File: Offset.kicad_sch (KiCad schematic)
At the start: 18 parts, among them J1 Conn_01x02, J2 Conn_01x02, J3 Conn_01x02, U1 LM358

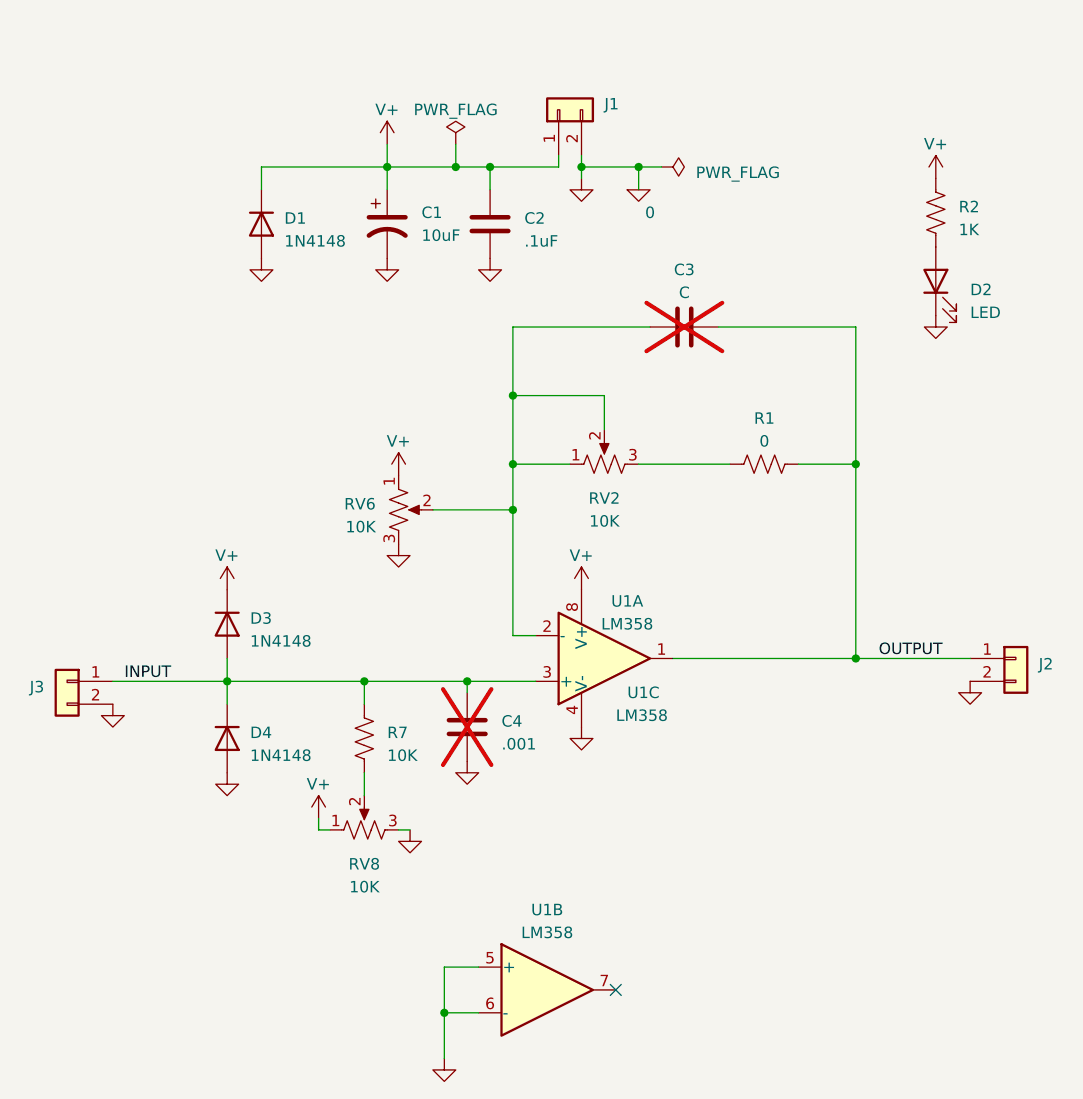
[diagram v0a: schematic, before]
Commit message: Remove zero reference
Seems to not be needed
Causes an ERC warning
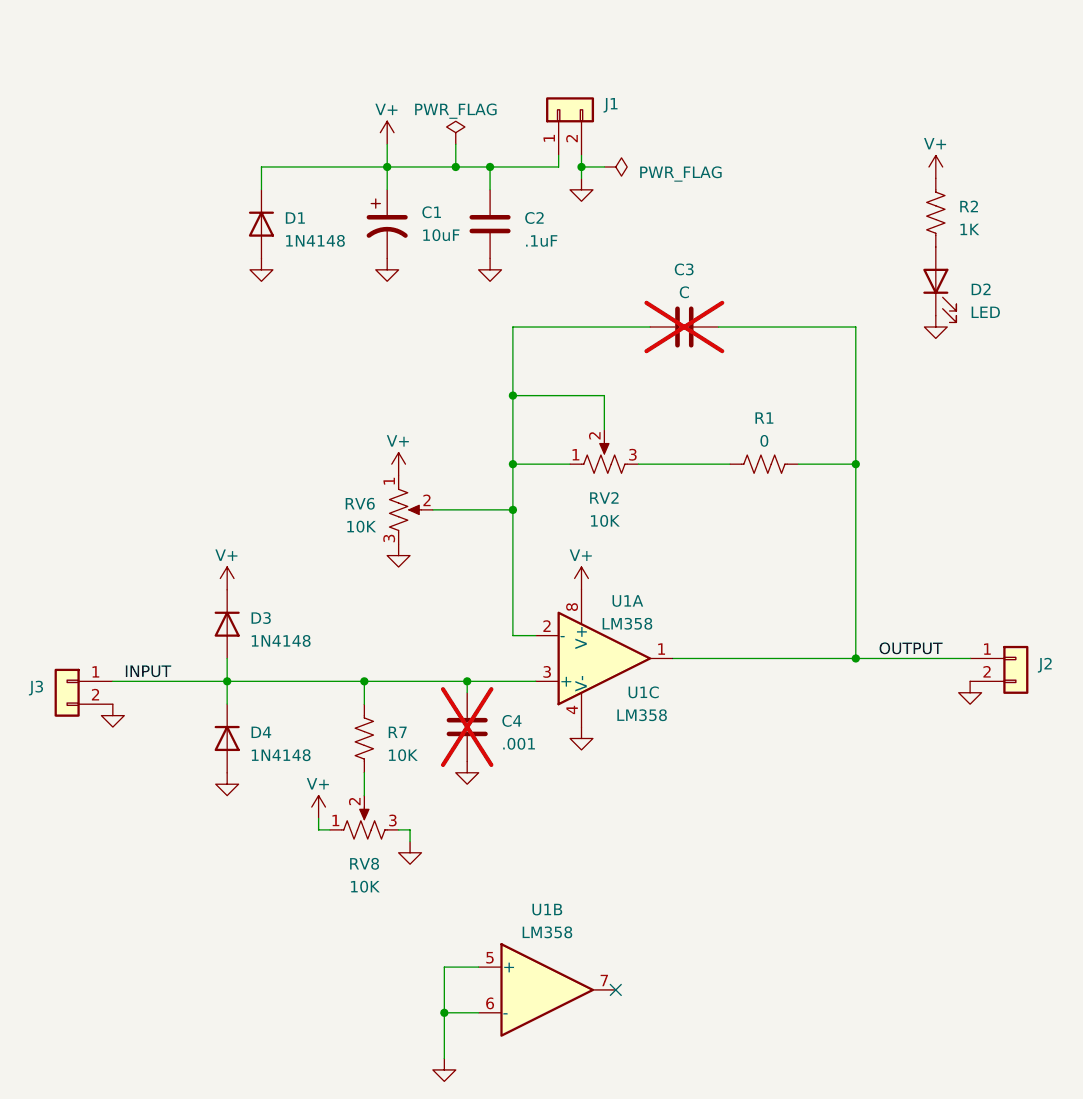
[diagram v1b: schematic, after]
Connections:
- net 0 renamed GND
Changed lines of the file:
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@@
   (junction (at 137.16 107.95) (diameter 0) (color 0 0 0 0)
-  )
-  (junction (at 156.21 50.8) (diameter 0) (color 0 0 0 0)
   )
   (junction (at 139.7 50.8) (diameter 0) (color 0 0 0 0)
@@
     (stroke (width 0) (type default))
   )
-  (wire (pts (xy 149.86 50.8) (xy 156.21 50.8))
+  (wire (pts (xy 149.86 50.8) (xy 152.4 50.8))
     (stroke (width 0) (type default))
   )
@@
     (stroke (width 0) (type default))
   )
+  (wire (pts (xy 130.81 124.46) (xy 130.81 125.73))
+    (stroke (width 0) (type default))
+  )
+  (wire (pts (xy 129.54 124.46) (xy 130.81 124.46))
+    (stroke (width 0) (type default))
+  )
   (wire (pts (xy 142.24 88.9) (xy 142.24 83.82))
     (stroke (width 0) (type default))
@@
     (stroke (width 0) (type default))
   )
-  (wire (pts (xy 156.21 50.8) (xy 158.75 50.8))
-    (stroke (width 0) (type default))
-  )
   (wire (pts (xy 180.34 83.82) (xy 180.34 105.41))
     (stroke (width 0) (type default))
@@
     (stroke (width 0) (type default))
   )
-  (wire (pts (xy 156.21 50.8) (xy 156.21 53.34))
-    (stroke (width 0) (type default))
-  )
   (wire (pts (xy 110.49 105.41) (xy 110.49 107.95))
     (stroke (width 0) (type default))
@@
   )
   (wire (pts (xy 142.24 68.58) (xy 142.24 76.2))
-    (stroke (width 0) (type default))
-  )
-  (wire (pts (xy 129.54 124.46) (xy 130.81 124.46))
     (stroke (width 0) (type default))
   )
@@
     )
   )
-  (symbol (lib_id "power:PWR_FLAG") (at 158.75 50.8 270) (unit 1)
-    (in_bom yes) (on_board yes) (dnp no) (fields_autoplaced)
-    (property "Reference" "#FLG01" (at 160.655 50.8 0)
-      (effects (font (size 1.27 1.27)) hide)
-    )
-    (property "Value" "PWR_FLAG" (at 162.56 51.435 90)
-      (effects (font (size 1.27 1.27)) (justify left))
-    )
-    (property "Footprint" "" (at 158.75 50.8 0)
-      (effects (font (size 1.27 1.27)) hide)
-    )
-    (property "Datasheet" "~" (at 158.75 50.8 0)
+  (symbol (lib_id "power:PWR_FLAG") (at 152.4 50.8 270) (unit 1)
+    (in_bom yes) (on_board yes) (dnp no) (fields_autoplaced)
+    (property "Reference" "#FLG01" (at 154.305 50.8 0)
+      (effects (font (size 1.27 1.27)) hide)
+    )
+    (property "Value" "PWR_FLAG" (at 156.21 51.435 90)
+      (effects (font (size 1.27 1.27)) (justify left))
+    )
+    (property "Footprint" "" (at 152.4 50.8 0)
+      (effects (font (size 1.27 1.27)) hide)
+    )
+    (property "Datasheet" "~" (at 152.4 50.8 0)
       (effects (font (size 1.27 1.27)) hide)
     )
@@
     )
   )
-  (symbol (lib_id "power:GND") (at 130.81 124.46 0) (unit 1)
-    (in_bom yes) (on_board yes) (dnp no) (fields_autoplaced)
-    (property "Reference" "#PWR010" (at 130.81 130.81 0)
-      (effects (font (size 1.27 1.27)) hide)
-    )
-    (property "Value" "GND" (at 130.81 129.54 0)
-      (effects (font (size 1.27 1.27)) hide)
-    )
-    (property "Footprint" "" (at 130.81 124.46 0)
-      (effects (font (size 1.27 1.27)) hide)
-    )
-    (property "Datasheet" "" (at 130.81 124.46 0)
+  (symbol (lib_id "power:VCC") (at 149.86 97.79 0) (unit 1)
+    (in_bom yes) (on_board yes) (dnp no) (fields_autoplaced)
+    (property "Reference" "#PWR02" (at 149.86 101.6 0)
+      (effects (font (size 1.27 1.27)) hide)
+    )
+    (property "Value" "V+" (at 149.86 93.98 0)
+      (effects (font (size 1.27 1.27)))
+    )
+    (property "Footprint" "" (at 149.86 97.79 0)
+      (effects (font (size 1.27 1.27)) hide)
+    )
+    (property "Datasheet" "" (at 149.86 97.79 0)
+      (effects (font (size 1.27 1.27)) hide)
+    )
+    (pin "1")
+    (instances
+      (project "Offset"
+        (path "/b9c335b0-b204-4837-ad88-f803b4ac701f"
+          (reference "#PWR02") (unit 1)
+        )
+      )
+    )
+  )
+  (symbol (lib_id "power:GND") (at 130.81 125.73 0) (unit 1)
+    (in_bom yes) (on_board yes) (dnp no) (fields_autoplaced)
+    (property "Reference" "#PWR010" (at 130.81 132.08 0)
+      (effects (font (size 1.27 1.27)) hide)
+    )
+    (property "Value" "GND" (at 130.81 130.81 0)
+      (effects (font (size 1.27 1.27)) hide)
+    )
+    (property "Footprint" "" (at 130.81 125.73 0)
+      (effects (font (size 1.27 1.27)) hide)
+    )
+    (property "Datasheet" "" (at 130.81 125.73 0)
       (effects (font (size 1.27 1.27)) hide)
     )
@@
         )
       )
-    )
-  )
-  (symbol (lib_id "power:VCC") (at 149.86 97.79 0) (unit 1)
-    (in_bom yes) (on_board yes) (dnp no) (fields_autoplaced)
-    (property "Reference" "#PWR02" (at 149.86 101.6 0)
-      (effects (font (size 1.27 1.27)) hide)
-    )
-    (property "Value" "V+" (at 149.86 93.98 0)
-      (effects (font (size 1.27 1.27)))
-    )
-    (property "Footprint" "" (at 149.86 97.79 0)
-      (effects (font (size 1.27 1.27)) hide)
-    )
-    (property "Datasheet" "" (at 149.86 97.79 0)
-      (effects (font (size 1.27 1.27)) hide)
-    )
-    (pin "1")
-    (instances
-      (project "Offset"
-        (path "/b9c335b0-b204-4837-ad88-f803b4ac701f"
-          (reference "#PWR02") (unit 1)
-        )
-      )
-    )
-  )
-  (symbol (lib_id "Simulation_SPICE:0") (at 156.21 53.34 0) (unit 1)
-    (in_bom yes) (on_board yes) (dnp no)
-    (property "Reference" "#GND01" (at 156.21 55.88 0)
-      (effects (font (size 1.27 1.27)) hide)
-    )
-    (property "Value" "0" (at 157.48 55.88 0)
-      (effects (font (size 1.27 1.27)))
-    )
-    (property "Footprint" "" (at 156.21 53.34 0)
-      (effects (font (size 1.27 1.27)) hide)
-    )
-    (property "Datasheet" "~" (at 156.21 53.34 0)
-      (effects (font (size 1.27 1.27)) hide)
-    )
-    (pin "1")
-    (instances
-      (project "Offset"
-        (path "/b9c335b0-b204-4837-ad88-f803b4ac701f"
-          (reference "#GND01") (unit 1)
-        )
-      )

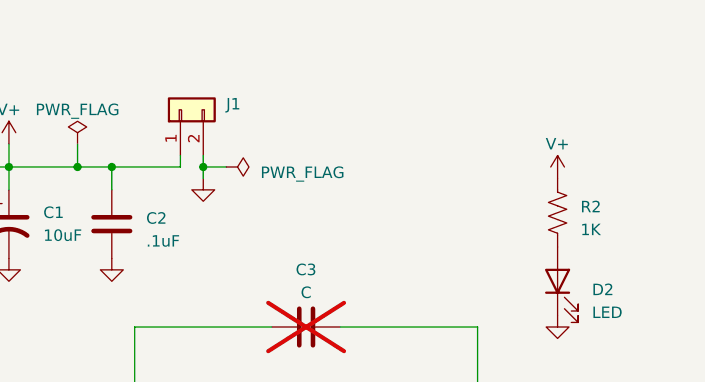
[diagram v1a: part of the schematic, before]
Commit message: Add power to simulation
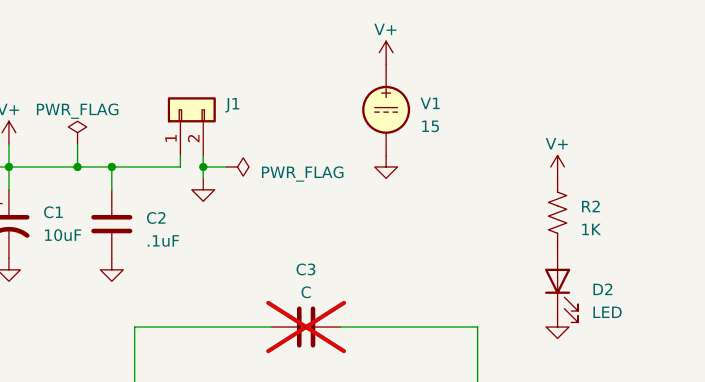
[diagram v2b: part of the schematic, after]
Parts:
- added V1: 15, symbol Simulation_SPICE:VDC
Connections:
- net GND: now also V1.2
- net VCC: now also V1.1
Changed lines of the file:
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@@
+    )
+  )
+  (symbol (lib_id "power:VCC") (at 170.18 39.37 0) (unit 1)
+    (in_bom yes) (on_board yes) (dnp no) (fields_autoplaced)
+    (property "Reference" "#PWR020" (at 170.18 43.18 0)
+      (effects (font (size 1.27 1.27)) hide)
+    )
+    (property "Value" "V+" (at 170.18 35.56 0)
+      (effects (font (size 1.27 1.27)))
+    )
+    (property "Footprint" "" (at 170.18 39.37 0)
+      (effects (font (size 1.27 1.27)) hide)
+    )
+    (property "Datasheet" "" (at 170.18 39.37 0)
+      (effects (font (size 1.27 1.27)) hide)
+    )
+    (pin "1")
+    (instances
+      (project "Offset"
+        (path "/b9c335b0-b204-4837-ad88-f803b4ac701f"
+          (reference "#PWR020") (unit 1)
+        )
+      )
     )
   )
@@
         (path "/b9c335b0-b204-4837-ad88-f803b4ac701f"
           (reference "RV6") (unit 1)
+        )
+      )
+    )
+  )
+  (symbol (lib_id "power:GND") (at 170.18 49.53 0) (unit 1)
+    (in_bom yes) (on_board yes) (dnp no) (fields_autoplaced)
+    (property "Reference" "#PWR021" (at 170.18 55.88 0)
+      (effects (font (size 1.27 1.27)) hide)
+    )
+    (property "Value" "GND" (at 170.18 54.61 0)
+      (effects (font (size 1.27 1.27)) hide)
+    )
+    (property "Footprint" "" (at 170.18 49.53 0)
+      (effects (font (size 1.27 1.27)) hide)
+    )
+    (property "Datasheet" "" (at 170.18 49.53 0)
+      (effects (font (size 1.27 1.27)) hide)
+    )
+    (pin "1")
+    (instances
+      (project "Offset"
+        (path "/b9c335b0-b204-4837-ad88-f803b4ac701f"
+          (reference "#PWR021") (unit 1)
         )
       )
@@
         )
       )
+    )
+  )
+  (symbol (lib_id "Simulation_SPICE:VDC") (at 170.18 44.45 0) (unit 1)
+    (in_bom yes) (on_board yes) (dnp no) (fields_autoplaced)
+    (property "Reference" "V1" (at 173.99 43.7792 0)
+      (effects (font (size 1.27 1.27)) (justify left))
+    )
+    (property "Value" "15" (at 173.99 46.3192 0)
+      (effects (font (size 1.27 1.27)) (justify left))
+    )
+    (property "Footprint" "" (at 170.18 44.45 0)
+      (effects (font (size 1.27 1.27)) hide)
+    )
+    (property "Datasheet" "~" (at 170.18 44.45 0)
+      (effects (font (size 1.27 1.27)) hide)
+    )
+    (property "Sim.Pins" "1=+ 2=-" (at 170.18 44.45 0)
+      (effects (font (size 1.27 1.27)) hide)
+    )
+    (property "Sim.Type" "DC" (at 170.18 44.45 0)
+      (effects (font (size 1.27 1.27)) hide)
+    )
+    (property "Sim.Device" "V" (at 170.18 44.45 0)
+      (effects (font (size 1.27 1.27)) (justify left) hide)
+    )
+    (pin "1")
+    (pin "2")
+    (instances
+      (project "Offset"
+        (path "/b9c335b0-b204-4837-ad88-f803b4ac701f"
+          (reference "V1") (unit 1)
+        )
+      )
